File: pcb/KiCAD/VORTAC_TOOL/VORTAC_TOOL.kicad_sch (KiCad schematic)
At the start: 6 parts, among them J1 Conn_01x05, J2 Conn_01x02, J3 Conn_01x03

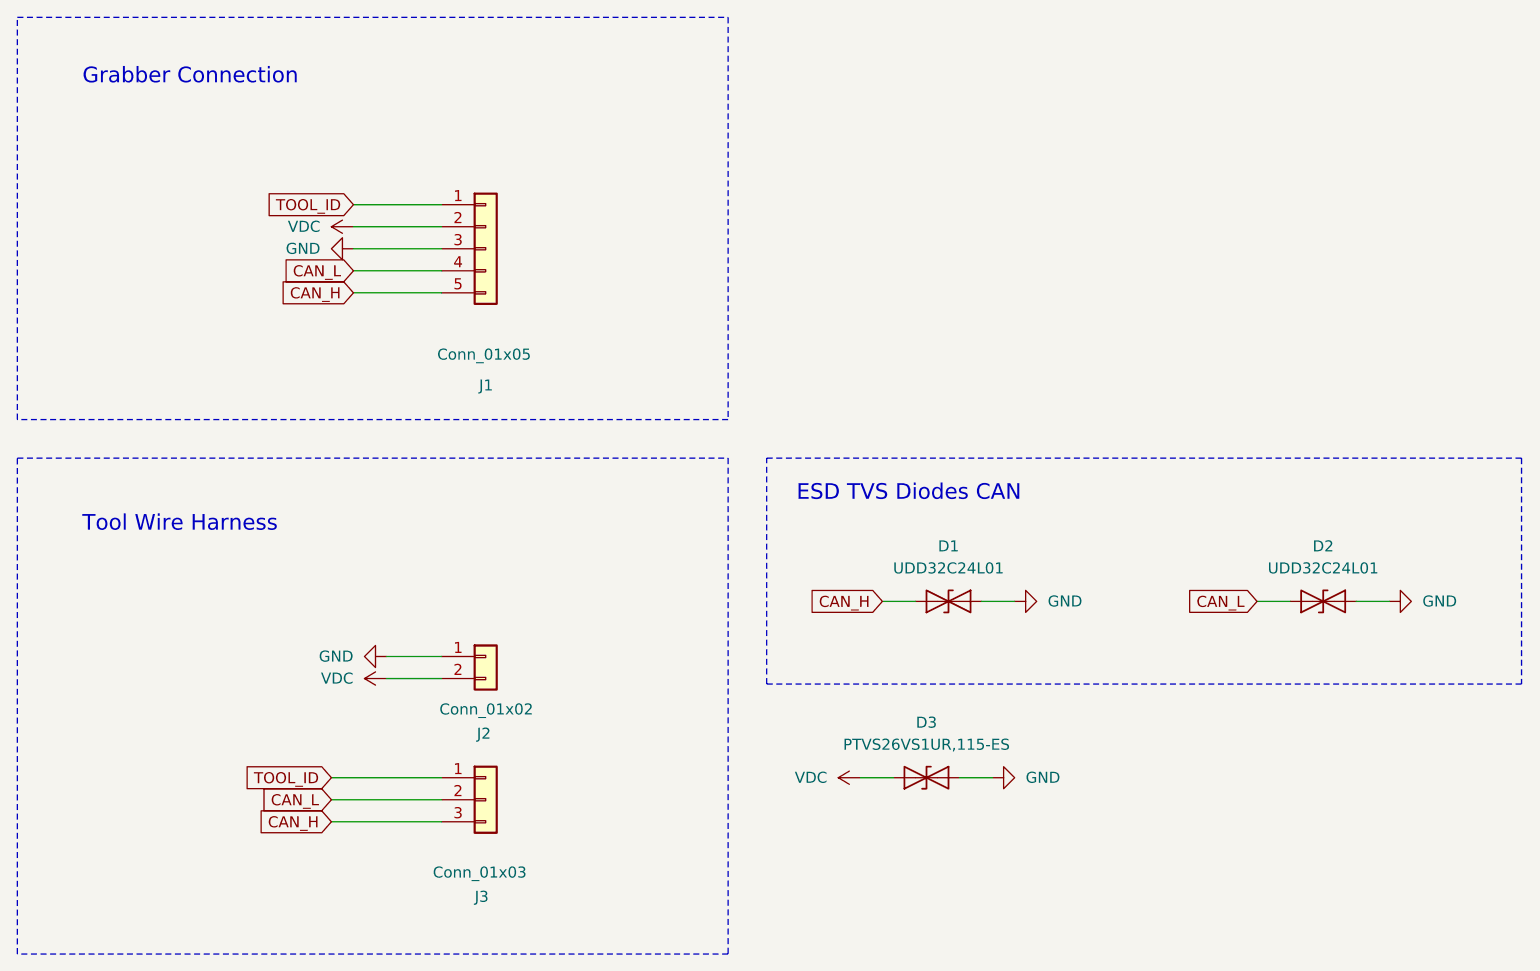
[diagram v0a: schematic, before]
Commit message: (Hopefully) Finalized DOCK, TOOL and TOOLPLATE REV2 for ordering
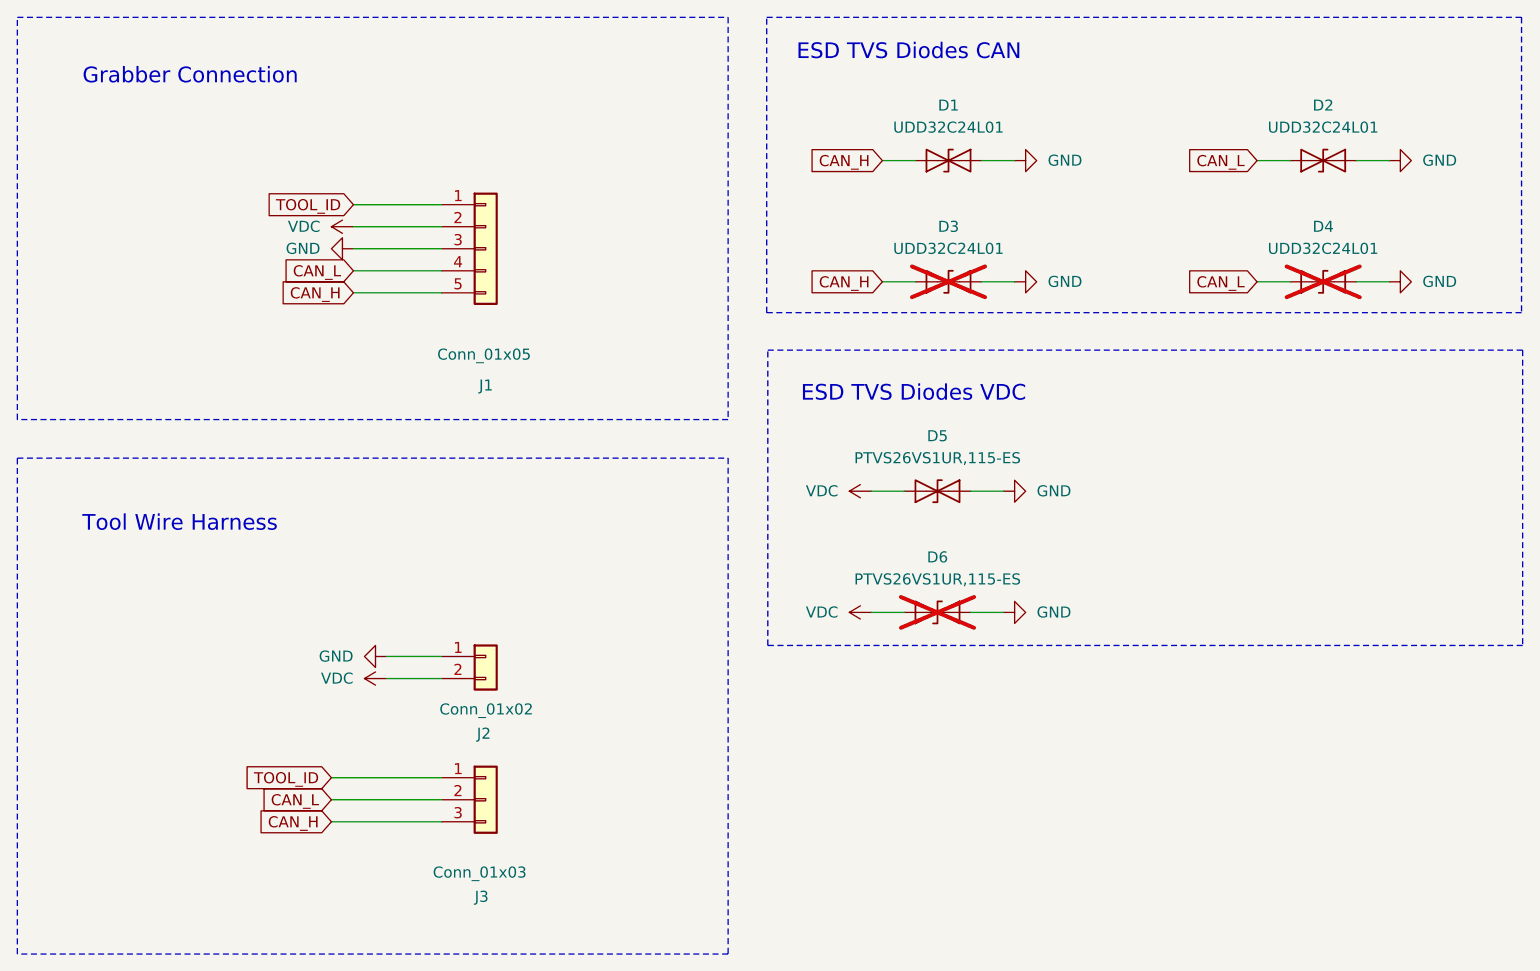
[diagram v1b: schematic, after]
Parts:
- added D3, D4: UDD32C24L01, Diode_SMD:D_SOD-323, symbol Diode:SD24_SOD323
- added D6: PTVS26VS1UR,115-ES, Diode_SMD:D_SOD-123F, symbol Diode:SD24_SOD323
- renumbered D3 to D5
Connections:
- net CAN_H: now also D3.2 (A2)
- net CAN_L: now also D4.2 (A2)
- net GND: now also D3.1 (A1), D4.1 (A1), D6.1 (A1)
- net VDC: now also D6.2 (A2)
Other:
- note added: "ESD TVS Diodes VDC"
- moved on the sheet: D1, D2, D5
